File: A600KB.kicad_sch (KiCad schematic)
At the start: 86 parts

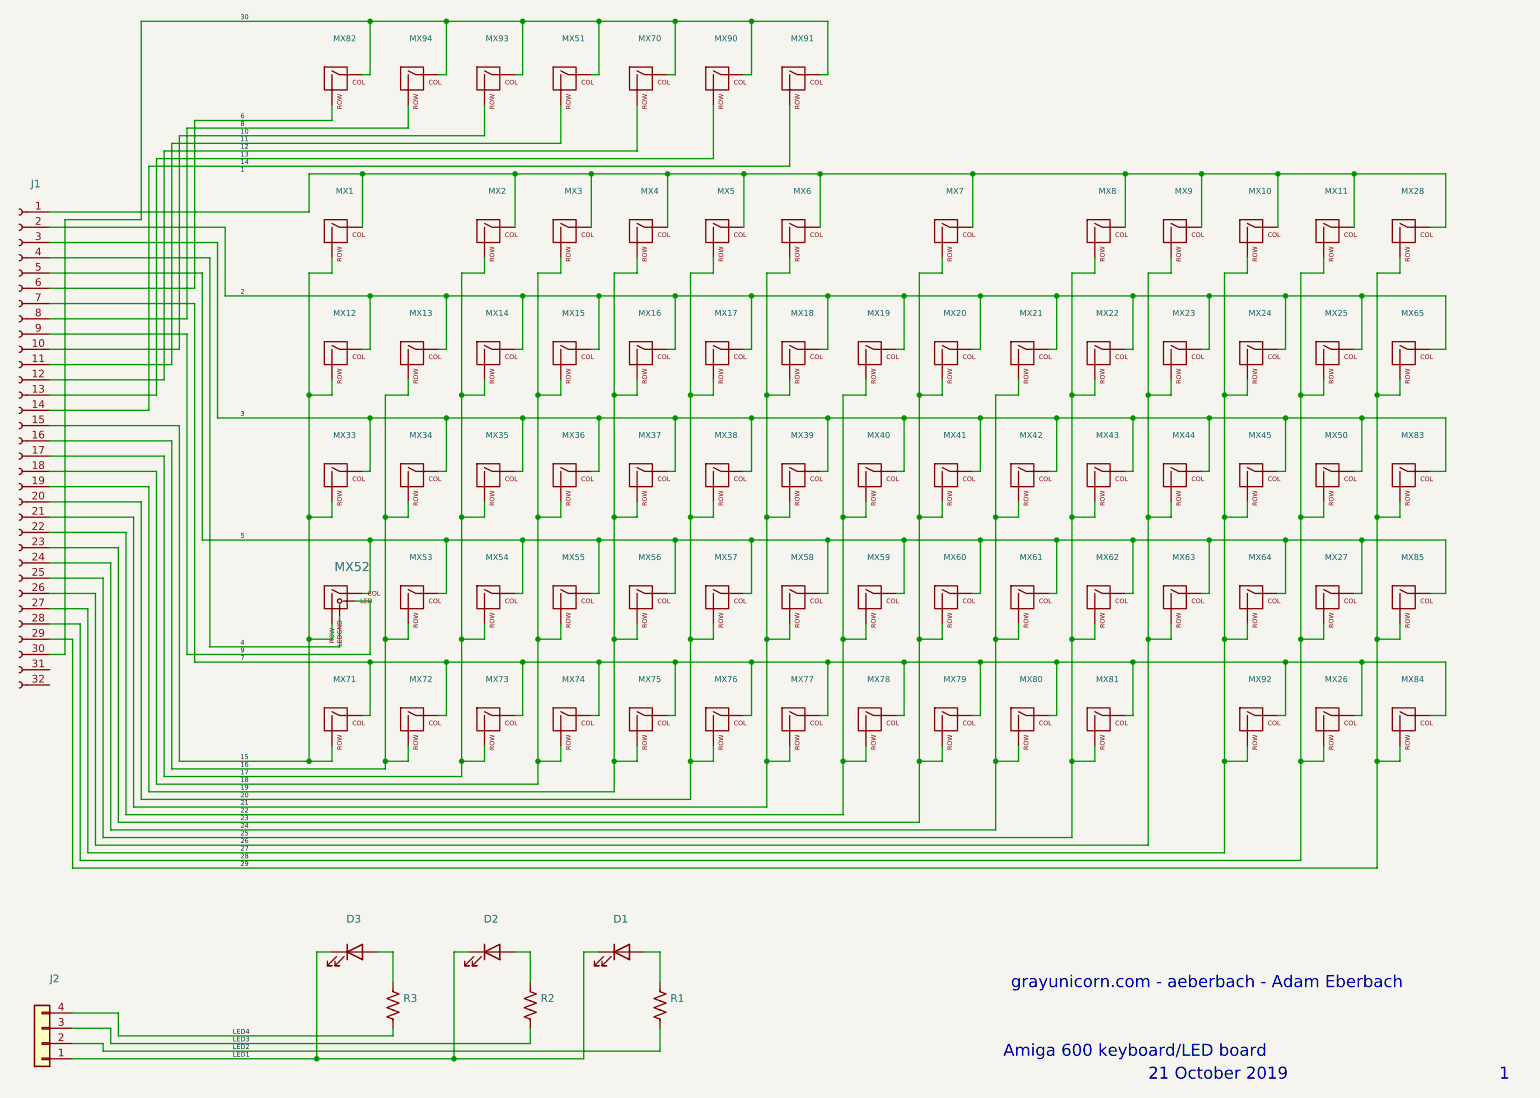
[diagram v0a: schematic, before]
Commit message: Revise PCB to fix swapped keys
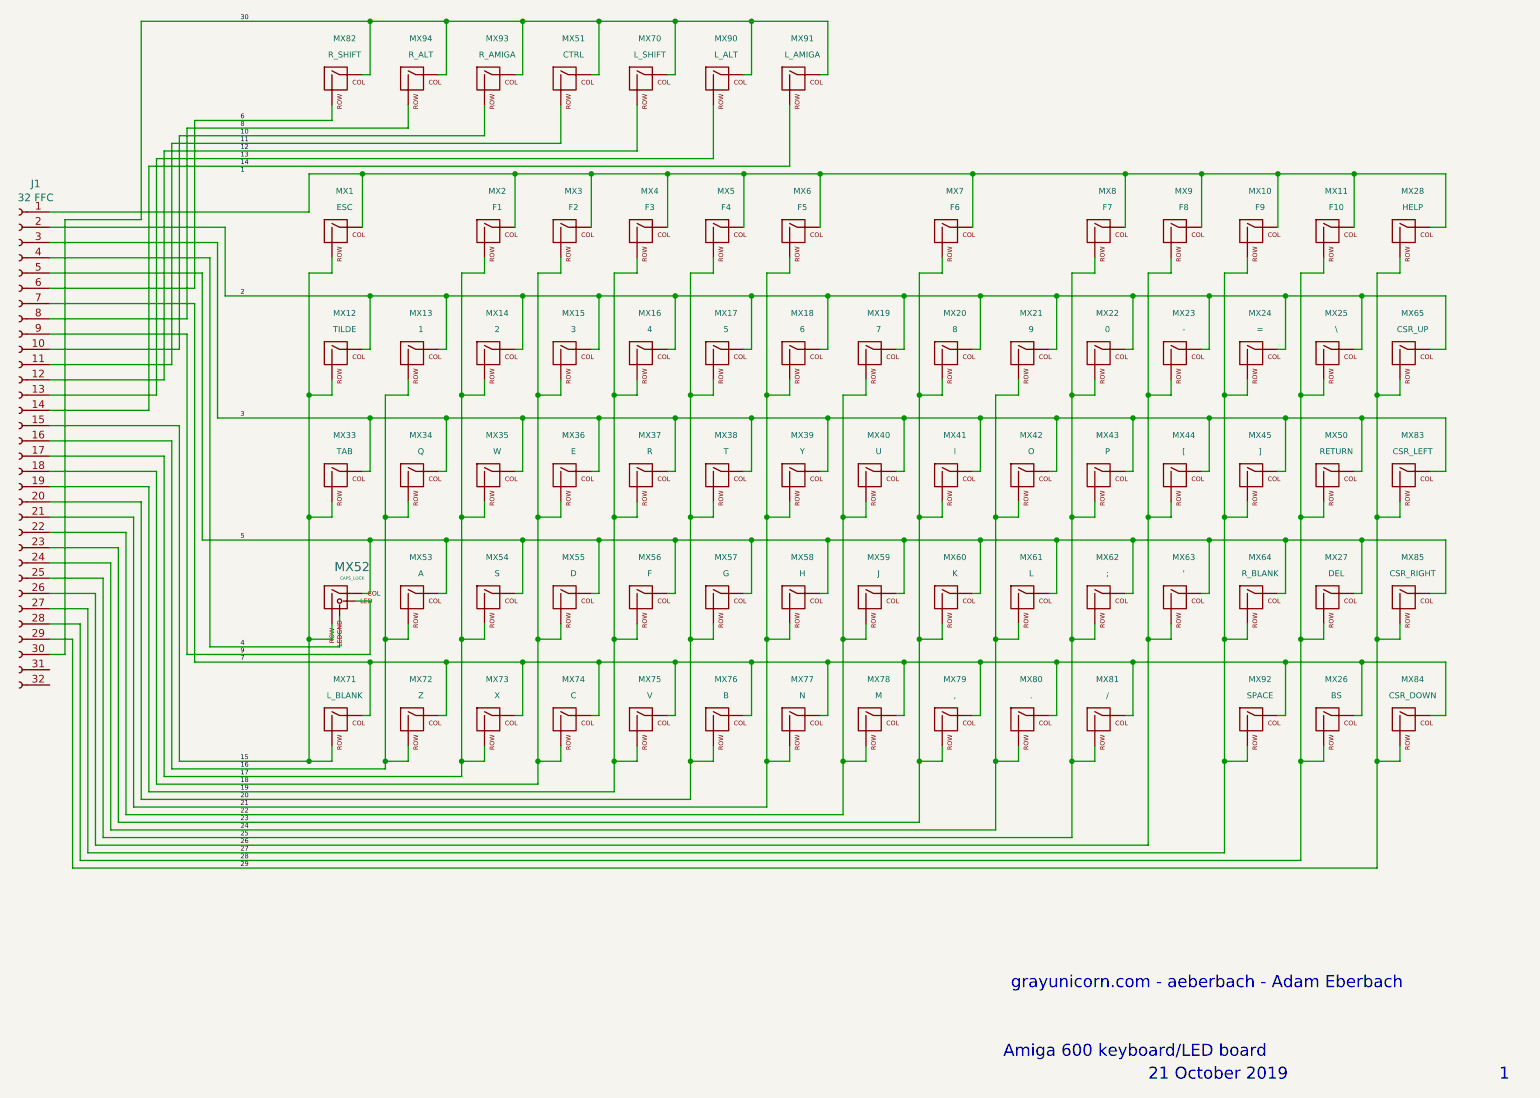
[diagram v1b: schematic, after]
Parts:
- removed D1, D2, D3: (no value), symbol Device:LED
- removed J2: (no value), symbol Connector_Generic:Conn_01x04
- removed R1, R2, R3: (no value), symbol Device:R_US
- J1: value (none) -> 32 FFC; footprint (none) -> A1200KB:FFC-1.25mm-RA-5204403245
- MX1: value (none) -> ESC; footprint (none) -> MX_Only:MXOnly-1.25U-NoLED
- MX10: value (none) -> F9; footprint (none) -> MX_Only:MXOnly-1.25U-NoLED
- MX11: value (none) -> F10; footprint (none) -> MX_Only:MXOnly-1.25U-NoLED
- MX12: value (none) -> TILDE; footprint (none) -> MX_Only:MXOnly-1.5U-NoLED
- MX13: value (none) -> 1; footprint (none) -> MX_Only:MXOnly-1U-NoLED
- MX14: value (none) -> 2; footprint (none) -> MX_Only:MXOnly-1U-NoLED
- MX15: value (none) -> 3; footprint (none) -> MX_Only:MXOnly-1U-NoLED
- MX16: value (none) -> 4; footprint (none) -> MX_Only:MXOnly-1U-NoLED
- MX17: value (none) -> 5; footprint (none) -> MX_Only:MXOnly-1U-NoLED
- MX18: value (none) -> 6; footprint (none) -> MX_Only:MXOnly-1U-NoLED
- MX19: value (none) -> 7; footprint (none) -> MX_Only:MXOnly-1U-NoLED
- MX2: value (none) -> F1; footprint (none) -> MX_Only:MXOnly-1.25U-NoLED
- MX20: value (none) -> 8; footprint (none) -> MX_Only:MXOnly-1U-NoLED
- MX21: value (none) -> 9; footprint (none) -> MX_Only:MXOnly-1U-NoLED
- MX22: value (none) -> 0; footprint (none) -> MX_Only:MXOnly-1U-NoLED
- MX23: value (none) -> -; footprint (none) -> MX_Only:MXOnly-1U-NoLED
- MX24: value (none) -> =; footprint (none) -> MX_Only:MXOnly-1U-NoLED
- MX25: value (none) -> \; footprint (none) -> MX_Only:MXOnly-1U-NoLED
- MX26: value (none) -> BS; footprint (none) -> MX_Only:MXOnly-1U-NoLED
- MX27: value (none) -> DEL; footprint (none) -> MX_Only:MXOnly-1U-NoLED
- MX28: value (none) -> HELP; footprint (none) -> MX_Only:MXOnly-1.25U-NoLED
- MX3: value (none) -> F2; footprint (none) -> MX_Only:MXOnly-1.25U-NoLED
- MX33: value (none) -> TAB; footprint (none) -> MX_Only:MXOnly-2U-NoLED
- MX34: value (none) -> Q; footprint (none) -> MX_Only:MXOnly-1U-NoLED
- MX35: value (none) -> W; footprint (none) -> MX_Only:MXOnly-1U-NoLED
- MX36: value (none) -> E; footprint (none) -> MX_Only:MXOnly-1U-NoLED
- MX37: value (none) -> R; footprint (none) -> MX_Only:MXOnly-1U-NoLED
- MX38: value (none) -> T; footprint (none) -> MX_Only:MXOnly-1U-NoLED
- MX39: value (none) -> Y; footprint (none) -> MX_Only:MXOnly-1U-NoLED
- MX4: value (none) -> F3; footprint (none) -> MX_Only:MXOnly-1.25U-NoLED
- MX40: value (none) -> U; footprint (none) -> MX_Only:MXOnly-1U-NoLED
- MX41: value (none) -> I; footprint (none) -> MX_Only:MXOnly-1U-NoLED
- MX42: value (none) -> O; footprint (none) -> MX_Only:MXOnly-1U-NoLED
- MX43: value (none) -> P; footprint (none) -> MX_Only:MXOnly-1U-NoLED
- MX44: value (none) -> [; footprint (none) -> MX_Only:MXOnly-1U-NoLED
- MX45: value (none) -> ]; footprint (none) -> MX_Only:MXOnly-1U-NoLED
- MX5: value (none) -> F4; footprint (none) -> MX_Only:MXOnly-1.25U-NoLED
- MX50: value (none) -> RETURN; footprint (none) -> MX_Only:MXOnly-ISO
- MX51: value (none) -> CTRL; footprint (none) -> MX_Only:MXOnly-1.25U-NoLED
- MX52: value (none) -> CAPS_LOCK; footprint (none) -> MX_Only:MXOnly-1U
- MX53: value (none) -> A; footprint (none) -> MX_Only:MXOnly-1U-NoLED
- MX54: value (none) -> S; footprint (none) -> MX_Only:MXOnly-1U-NoLED
- MX55: value (none) -> D; footprint (none) -> MX_Only:MXOnly-1U-NoLED
- MX56: value (none) -> F; footprint (none) -> MX_Only:MXOnly-1U-NoLED
- MX57: value (none) -> G; footprint (none) -> MX_Only:MXOnly-1U-NoLED
- MX58: value (none) -> H; footprint (none) -> MX_Only:MXOnly-1U-NoLED
- MX59: value (none) -> J; footprint (none) -> MX_Only:MXOnly-1U-NoLED
- MX6: value (none) -> F5; footprint (none) -> MX_Only:MXOnly-1.25U-NoLED
- MX60: value (none) -> K; footprint (none) -> MX_Only:MXOnly-1U-NoLED
- MX61: value (none) -> L; footprint (none) -> MX_Only:MXOnly-1U-NoLED
- MX62: value (none) -> ;; footprint (none) -> MX_Only:MXOnly-1U-NoLED
- MX63: value (none) -> '; footprint (none) -> MX_Only:MXOnly-1U-NoLED
- MX64: value (none) -> R_BLANK; footprint (none) -> MX_Only:MXOnly-1U-NoLED
- MX65: value (none) -> CSR_UP; footprint (none) -> MX_Only:MXOnly-1U-NoLED
- MX7: value (none) -> F6; footprint (none) -> MX_Only:MXOnly-1.25U-NoLED
- MX70: value (none) -> L_SHIFT; footprint (none) -> MX_Only:MXOnly-1.75U-NoLED
- MX71: value (none) -> L_BLANK; footprint (none) -> MX_Only:MXOnly-1U-NoLED
- MX72: value (none) -> Z; footprint (none) -> MX_Only:MXOnly-1U-NoLED
- MX73: value (none) -> X; footprint (none) -> MX_Only:MXOnly-1U-NoLED
- MX74: value (none) -> C; footprint (none) -> MX_Only:MXOnly-1U-NoLED
- MX75: value (none) -> V; footprint (none) -> MX_Only:MXOnly-1U-NoLED
- MX76: value (none) -> B; footprint (none) -> MX_Only:MXOnly-1U-NoLED
- MX77: value (none) -> N; footprint (none) -> MX_Only:MXOnly-1U-NoLED
- MX78: value (none) -> M; footprint (none) -> MX_Only:MXOnly-1U-NoLED
- MX79: value (none) -> ,; footprint (none) -> MX_Only:MXOnly-1U-NoLED
- MX8: value (none) -> F7; footprint (none) -> MX_Only:MXOnly-1.25U-NoLED
- MX80: value (none) -> .; footprint (none) -> MX_Only:MXOnly-1U-NoLED
- MX81: value (none) -> /; footprint (none) -> MX_Only:MXOnly-1U-NoLED
- MX82: value (none) -> R_SHIFT; footprint (none) -> MX_Only:MXOnly-1.75U-NoLED
- MX83: value (none) -> CSR_LEFT; footprint (none) -> MX_Only:MXOnly-1U-NoLED
- MX84: value (none) -> CSR_DOWN; footprint (none) -> MX_Only:MXOnly-1U-NoLED
- MX85: value (none) -> CSR_RIGHT; footprint (none) -> MX_Only:MXOnly-1U-NoLED
- MX9: value (none) -> F8; footprint (none) -> MX_Only:MXOnly-1.25U-NoLED
- MX90: value (none) -> L_ALT; footprint (none) -> MX_Only:MXOnly-1.25U-NoLED
- MX91: value (none) -> L_AMIGA; footprint (none) -> MX_Only:MXOnly-1.25U-NoLED
- MX92: value (none) -> SPACE; footprint (none) -> MX_Only:MXOnly-7U
- MX93: value (none) -> R_AMIGA; footprint (none) -> MX_Only:MXOnly-1.25U-NoLED
- MX94: value (none) -> R_ALT; footprint (none) -> MX_Only:MXOnly-1U-NoLED
